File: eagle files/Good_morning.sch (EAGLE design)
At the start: 67 parts, among them J2 20329, Q1 mmbt2222, Q2 mmbt2222, SW1 K2-1817UQ-C4SW-01, SW2 KMR2, U1 DRV8825PWP, U2 AP2112-3.3, U3 VEML6030, U4 ESP32_WROOM32_SKINNY, U5 CP2104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

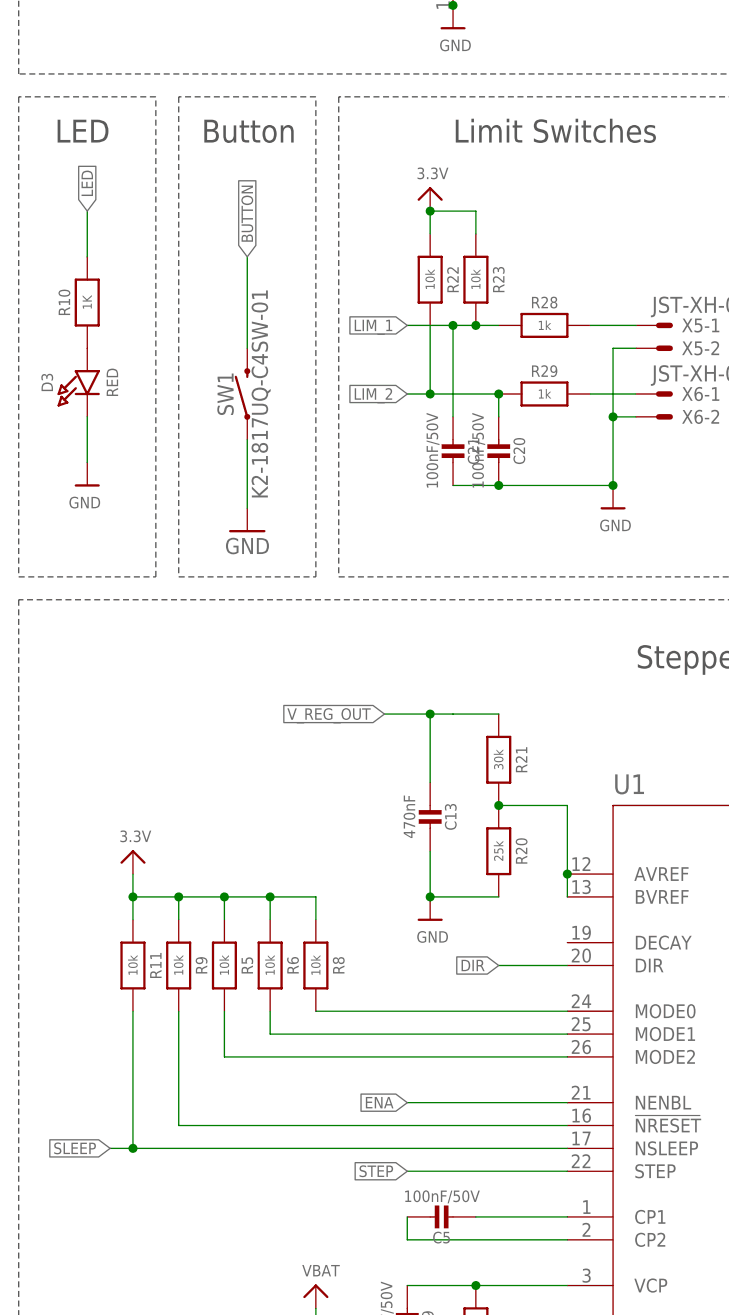
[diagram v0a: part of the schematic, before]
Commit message: fixes mentioned in readme errata
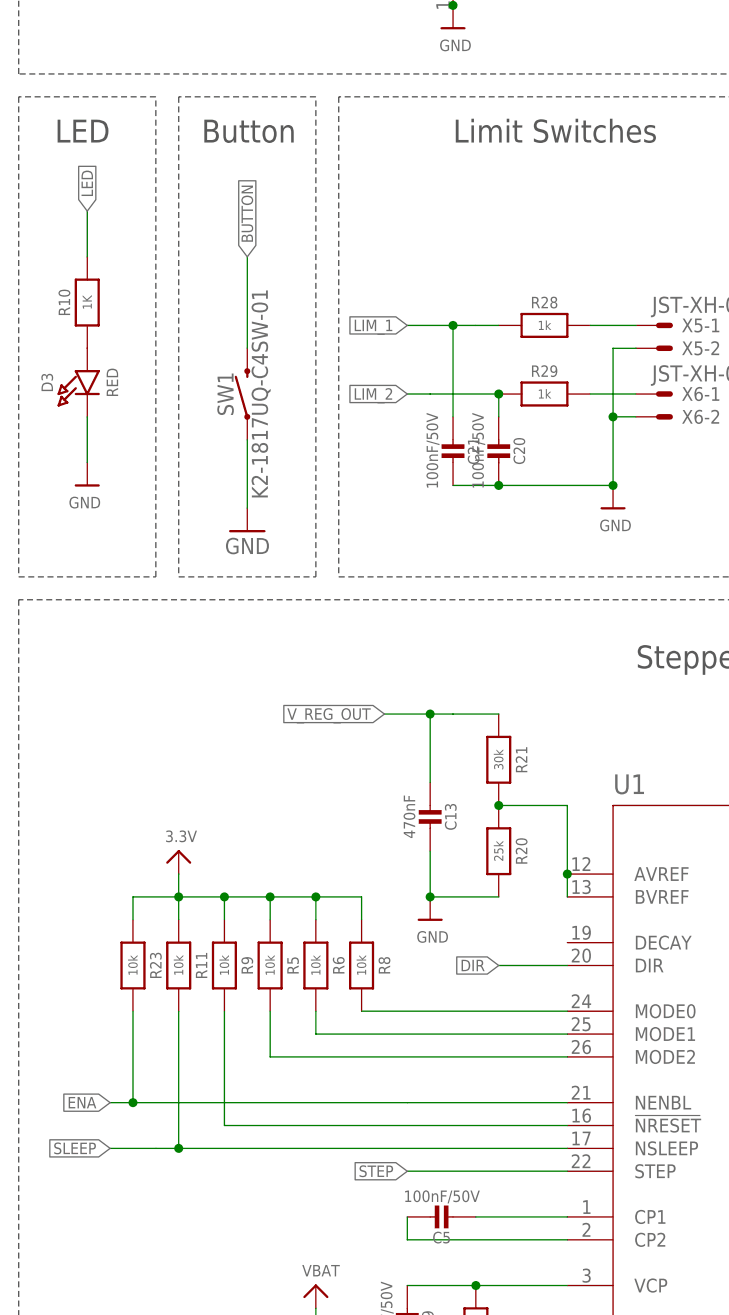
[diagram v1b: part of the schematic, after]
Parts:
- removed R22: 10k, microbuilder:RESISTOR_0402
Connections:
- net 3.3V: no longer R22.1
- net ENA: now also R23.2
- net LIM_1: no longer R23.2
- net LIM_2: no longer R22.2
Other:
- moved on the sheet: R11, R23, R5, R6, R8, R9
